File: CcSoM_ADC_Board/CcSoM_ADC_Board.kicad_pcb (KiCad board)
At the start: 4 copper layers, 160 x 100 mm, 158 parts, among them J1 SoM Connector, J12 USB_C_Receptacle_USB2.0_16P, J13 Conn_02x03_Odd_Even, J14 Conn_02x03_Odd_Even, J15 Conn_02x02_Counter_Clockwise, J16 Barrel_Jack, J18 USB_A, J19 USB_A, J3 Conn_02x8_Odd_Even, J4 Conn_Coaxial, J5 HR911130A1, J6 Conn_01x14, J7 Conn_01x08, J8 Conn_01x16_Socket, J9 Conn_01x08, SW3 SW_Push, U1 SN74LVC00APWE4, U10 USB3343, U11 RTL8211E-VB-CG, U14 SN74CB3T3306DCTR, U2 74AUP1G04, U3 93LC46B, U4 FT2232HL, U5 SN74CB3T3245PWR, U6 TPS73625DBV, U7 TPS3307-33DR, U8 TPS73633DBV, X1 12MHz, Y1 25MHz

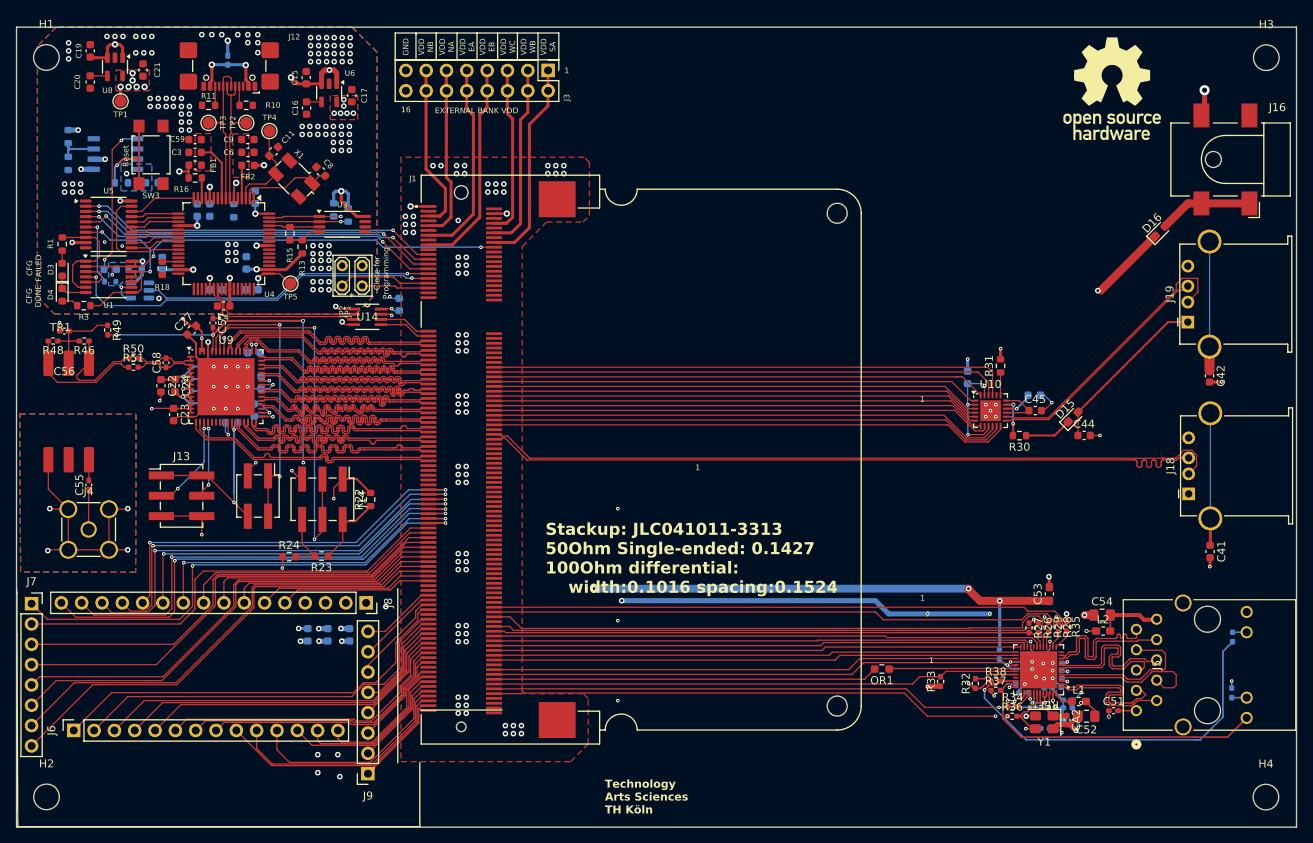
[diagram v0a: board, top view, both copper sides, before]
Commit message: changed from 10Bit ADC to 12Bit
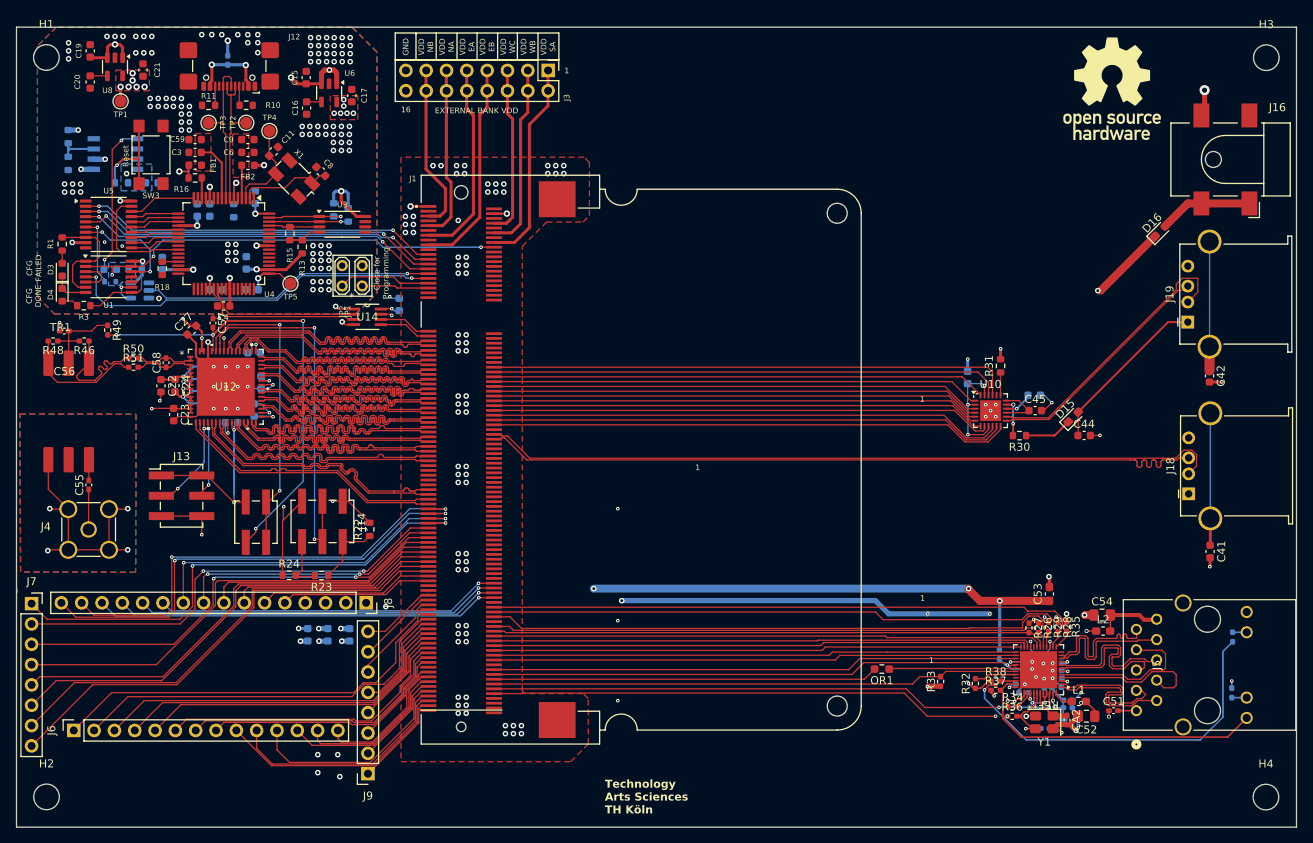
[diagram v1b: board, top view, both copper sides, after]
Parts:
- removed U9: ~, Package_DFN_QFN:QFN-64-1EP_9x9mm_P0.5mm_EP7.15x7.15mm
- added U12: LTC2242IUP-12-PBF, LTC2242-12:QFN-64_UP_LIT, F.Cu at (93.3, 95.5)
- moved R22 3.73 mm to (111.2, 113.3)
- moved J15 3.27 mm to (97.0, 112.4)
- moved J14 2.77 mm to (105.3, 112.3)
- moved R23 2.44 mm to (105.2, 119.1)
- moved R24 2.33 mm to (101.2, 119.1)
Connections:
- J1 pad 107: SB0_N -> D0_P
- J1 pad 109: SB0_P -> D0_N
- J1 pad 111: SB1_N -> OSC_N
- J1 pad 113: SB1_P -> OSC_P
- J1 pad 146: unconnected-(J1D-EB1_P-Pad146) -> EB1_P
- J1 pad 148: unconnected-(J1D-EB1_N-Pad148) -> EB1_N
- J1 pad 150: unconnected-(J1D-EB3_P-Pad150) -> EB3_P
- J1 pad 152: unconnected-(J1D-EB3_N-Pad152) -> EB3_N
- J1 pad 45: OF_N -> OF_P
- J1 pad 47: OF_P -> OF_N
- J1 pad 49: D9_P -> D11_P
- J1 pad 51: D9_N -> D11_N
- J1 pad 53: D8_P -> D10_P
- J1 pad 55: D8_N -> D10_N
- J1 pad 57: D7_P -> D9_P
- J1 pad 59: D7_N -> D9_N
- J1 pad 61: D6_P -> D8_P
- J1 pad 63: D6_N -> D8_N
- J1 pad 65: D5_P -> D7_P
- J1 pad 67: D5_N -> D7_N
- J1 pad 69: D4_P -> D6_P
- J1 pad 71: D4_N -> D6_N
- J1 pad 73: D3_P -> D5_P
- J1 pad 75: D3_N -> D5_N
- J1 pad 81: D2_P -> D4_P
- J1 pad 83: D2_N -> D4_N
- J1 pad 85: D1_P -> D3_P
- J1 pad 87: D1_N -> D3_N
- J1 pad 89: D0_P -> D2_P
- J1 pad 91: D0_N -> D2_N
- J1 pad 93: OSC_N -> D1_P
- J1 pad 95: OSC_P -> D1_N
- J15 pad 3: V_CM -> OVDD
- J15 pad 4: OVDD -> V_CM
- J8 pad 11: SB1_P -> EB1_P
- J8 pad 12: SB0_N -> EB1_N
- J8 pad 13: SB0_P -> EB3_P
- J8 pad 14: SB1_N -> EB3_N
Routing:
- net SB1_N: track 55.5 -> 0.00 mm, vias 2 -> 0
- net SB0_P: track 53.3 -> 0.00 mm, vias 2 -> 0
- net EB3_N: track 0.00 -> 50.6 mm, vias 0 -> 1
- net SB0_N: track 49.7 -> 0.00 mm, vias 2 -> 0
- net EB3_P: track 0.00 -> 48.2 mm, vias 0 -> 1
- net SB1_P: track 46.1 -> 0.00 mm, vias 2 -> 0
- net EB1_N: track 0.00 -> 45.7 mm, vias 0 -> 1
- net EB1_P: track 0.00 -> 43.2 mm, vias 0 -> 1
- net D11_P: track 0.00 -> 33.5 mm
- net D11_N: track 0.00 -> 33.5 mm
- net D10_P: track 0.00 -> 33.5 mm
- net D10_N: track 0.00 -> 33.5 mm
- net OGND: track 109.2 -> 117.8 mm, vias 259 -> 258
- net V_CM: track 54.0 -> 59.4 mm, vias 5 -> 4
- net BAL_P: track 13.1 -> 15.6 mm
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
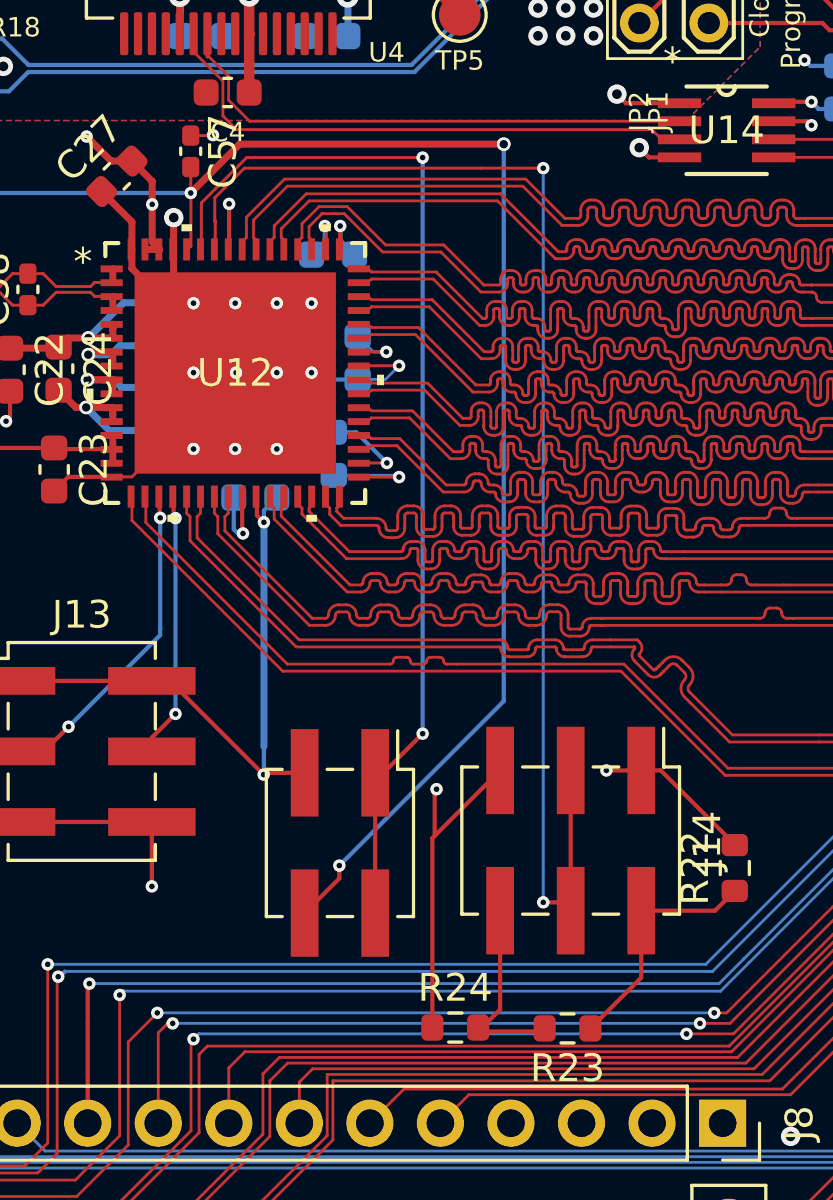
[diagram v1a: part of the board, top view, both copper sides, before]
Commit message: changed some traces
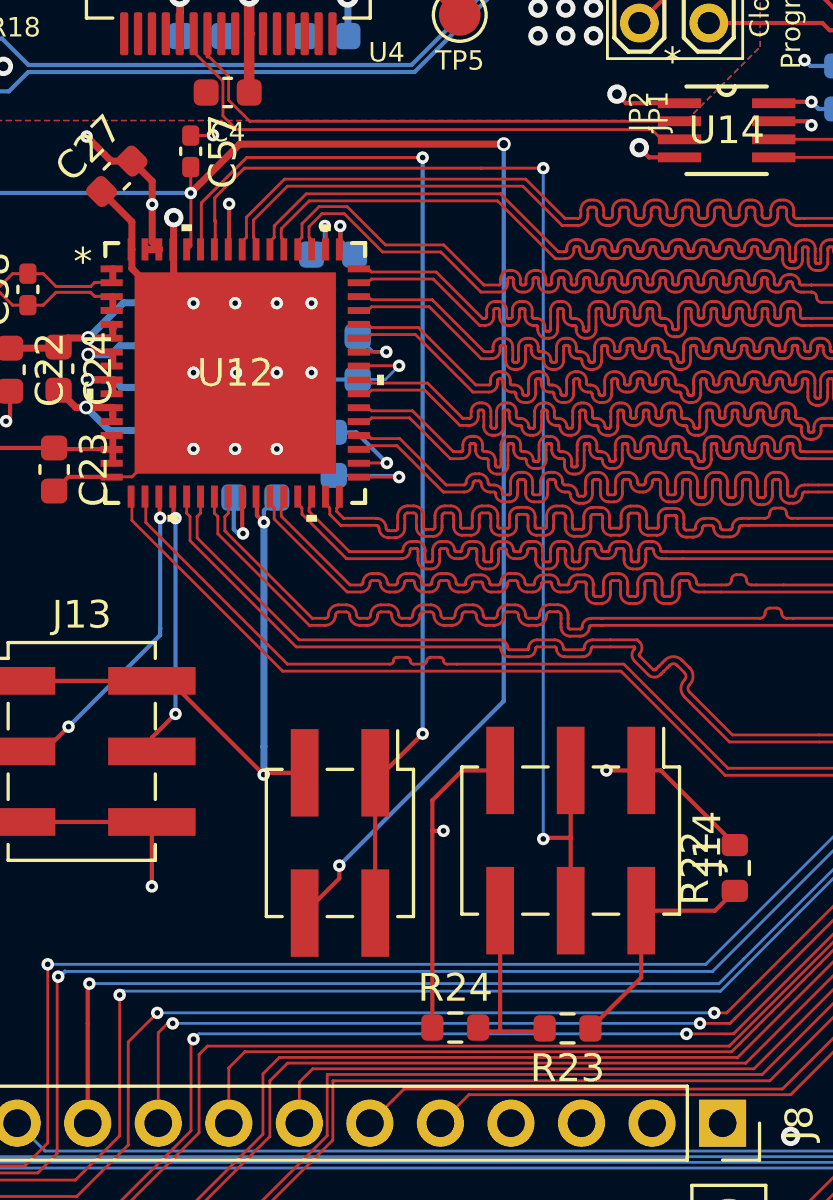
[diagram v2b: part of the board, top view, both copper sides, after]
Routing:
- net Net-(J14-Pin_3): track 46.8 -> 44.8 mm
- net OGND: track 117.8 -> 117.3 mm
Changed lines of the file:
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@@
 		(start 94.284667 108.965333)
 		(end 94.284667 109.965333)
-		(width 0.1524)
+		(width 0.254)
 		(layer "B.Cu")
 		(net 16)
@@
 		(start 97.031879 90.221452)
 		(end 98.691879 91.881452)
-		(width 0.1524)
+		(width 0.254)
 		(layer "In2.Cu")
 		(net 16)
@@
 		(start 92.68133 100.888933)
 		(end 92.160131 101.410131)
-		(width 0.1524)
+		(width 0.254)
 		(layer "In2.Cu")
 		(net 16)
@@
 		(start 91.5 105.25)
 		(end 94.25 108)
-		(width 0.1524)
+		(width 0.635)
 		(layer "In2.Cu")
 		(net 16)
@@
 	)
 	(segment
+		(start 106.614046 109.823942)
+		(end 94.426058 109.823942)
+		(width 0.635)
+		(layer "In2.Cu")
+		(net 16)
+	)
+	(segment
 		(start 82.8535 79.8232)
 		(end 82.8535 81.334114)
@@
 		(start 88.5 105.25)
 		(end 91.5 105.25)
-		(width 0.1524)
+		(width 0.635)
 		(layer "In2.Cu")
 		(net 16)
@@
 	)
 	(segment
-		(start 106.615946 109.825842)
-		(end 94.424158 109.825842)
-		(width 0.1524)
-		(layer "In2.Cu")
-		(net 16)
-	)
-	(segment
 		(start 94.25 109.95)
 		(end 94.275 109.975)
@@
 		(start 97.741455 100.888933)
 		(end 98.711879 99.918509)
-		(width 0.1524)
+		(width 0.254)
 		(layer "In2.Cu")
 		(net 16)
@@
 		(start 94.25 108)
 		(end 94.25 109.95)
-		(width 0.1524)
+		(width 0.635)
 		(layer "In2.Cu")
 		(net 16)
@@
 		(start 98.711879 99.918509)
 		(end 98.711879 98.754)
-		(width 0.1524)
+		(width 0.254)
 		(layer "In2.Cu")
 		(net 16)
@@
 		(start 98.691879 91.881452)
 		(end 98.691879 94.754)
-		(width 0.1524)
+		(width 0.254)
+		(layer "In2.Cu")
+		(net 16)
+	)
+	(segment
+		(start 94.426058 109.823942)
+		(end 94.424158 109.825842)
+		(width 0.635)
 		(layer "In2.Cu")
 		(net 16)
@@
 		(start 94.284667 100.888933)
 		(end 97.741455 100.888933)
-		(width 0.1524)
+		(width 0.254)
 		(layer "In2.Cu")
 		(net 16)
@@
 	)
 	(segment
+		(start 106.615946 109.825842)
+		(end 106.614046 109.823942)
+		(width 0.635)
+		(layer "In2.Cu")
+		(net 16)
+	)
+	(segment
 		(start 94.284667 100.888933)
 		(end 92.68133 100.888933)
-		(width 0.1524)
+		(width 0.254)
 		(layer "In2.Cu")
 		(net 16)
@@
 		(start 92.160131 101.410131)
 		(end 84.666751 101.410131)
-		(width 0.1524)
+		(width 0.635)
 		(layer "In2.Cu")
 		(net 16)
@@
 		(start 84.663441 101.413441)
 		(end 88.5 105.25)
-		(width 0.1524)
+		(width 0.635)
 		(layer "In2.Cu")
 		(net 16)
@@
 		(start 98.691879 94.754)
 		(end 98.691879 98.734)
-		(width 0.1524)
+		(width 0.254)
 		(layer "In2.Cu")
 		(net 16)
@@
 	)
 	(segment
+		(start 102.7902 109.824223)
+		(end 101.425777 109.824223)
+		(width 0.1524)
+		(layer "F.Cu")
+		(net 17)
+	)
+	(segment
 		(start 91.031879 89.925404)
 		(end 91.037581 89.919702)
@@
 	)
 	(segment
-		(start 100.432211 112.182211)
-		(end 100.432211 110.567789)
-		(width 0.1524)
-		(layer "F.Cu")
-		(net 17)
-	)
-	(segment
 		(start 85.144132 96.170487)
 		(end 85.144132 97.105868)
@@
 	)
 	(segment
-		(start 100.432211 110.567789)
-		(end 100.5 110.5)
-		(width 0.1524)
-		(layer "F.Cu")
-		(net 17)
-	)
-	(segment
 		(start 191.005 134.755)
 		(end 191 134.75)
@@
 	)
 	(segment
-		(start 100.35 119.223048)
-		(end 100.35 112.264423)
-		(width 0.1524)
-		(layer "F.Cu")
-		(net 17)
-	)
-	(segment
 		(start 194.462966 136.66377)
 		(end 193.33623 136.66377)
@@
 	)
 	(segment
-		(start 100.432211 112.182211)
-		(end 102.7902 109.824223)
-		(width 0.1524)
-		(layer "F.Cu")
-		(net 17)
-	)
-	(segment
 		(start 188.9 133.45)
 		(end 188.9 133.75)
@@
 	)
 	(segment
+		(start 100.35 112)
+		(end 100.75 112)
+		(width 0.1524)
+		(layer "F.Cu")
+		(net 17)
+	)
+	(segment
 		(start 216.287337 117.962663)
 		(end 216.25 118)
@@
 	)
 	(segment
+		(start 101.425777 109.824223)
+		(end 100.35 110.9)
+		(width 0.1524)
+		(layer "F.Cu")
+		(net 17)
+	)
+	(segment
 		(start 196.2 120.55)
 		(end 196.2 119.3)
@@
 	)
 	(segment
+		(start 100.35 110.9)
+		(end 100.35 112)
+		(width 0.1524)
+		(layer "F.Cu")
+		(net 17)
+	)
+	(segment
 		(start 88.844379 99.254)
 		(end 87.240789 99.254)
@@
 	)
 	(segment
-		(start 100.35 112.264423)
-		(end 100.432211 112.182211)
-		(width 0.1524)
-		(layer "F.Cu")
-		(net 17)
-	)
-	(segment
 		(start 96.531879 90.273055)
 		(end 96.480276 90.221452)
@@
 	)
 	(segment
+		(start 100.35 112)
+		(end 100.35 119.223048)
+		(width 0.1524)
+		(layer "F.Cu")
+		(net 17)
+	)
+	(segment
 		(start 113.8559 86.45)
 		(end 114 86.5941)
@@
 	)
 	(via
-		(at 100.5 110.5)
-		(size 0.45)
-		(drill 0.2)
-		(layers "F.Cu" "B.Cu")
-		(net 17)
-	)
-	(via
 		(at 104.8535 54.8732)
 		(size 0.7)
@@
 	)
 	(via
+		(at 100.75 112)
+		(size 0.45)
+		(drill 0.2)
+		(layers "F.Cu" "B.Cu")
+		(net 17)
+	)
+	(via
 		(at 123.3035 126.3732)
 		(size 0.7)
@@
 	)
 	(segment
+		(start 104.384521 112.25)
+		(end 104.3432 112.291321)
+		(width 0.1524)
+		(layer "F.Cu")
+		(net 119)
+	)
+	(segment
 		(start 92.531879 91.0665)
 		(end 92.511879 91.0465)
@@
 	(segment
 		(start 105.3302 109.824223)
-		(end 105.3302 114.874223)
-		(width 0.1524)
-		(layer "F.Cu")
-		(net 119)
-	)
-	(segment
-		(start 104.3432 114.574552)
-		(end 105.030529 114.574552)
+		(end 105.3302 112.25)
 		(width 0.1524)
 		(layer "F.Cu")
@@
 	)
 	(segment
+		(start 105.3302 112.25)
+		(end 105.3302 114.874223)
+		(width 0.1524)
+		(layer "F.Cu")
+		(net 119)
+	)
+	(segment
 		(start 92.515177 89.204117)
 		(end 93.581294 88.138)
@@
 	)
 	(segment
+		(start 105.3302 112.25)
+		(end 104.384521 112.25)
+		(width 0.1524)
+		(layer "F.Cu")
+		(net 119)
+	)
+	(segment
 		(start 92.531879 90.043)
 		(end 92.515177 90.026298)
@@
 	)
 	(via
-		(at 104.3432 114.574552)
+		(at 104.3432 112.291321)
 		(size 0.45)
 		(drill 0.2)
@@
 	)
 	(segment
+		(start 104.3432 112.291321)
+		(end 104.347033 112.295154)
+		(width 0.108204)
+		(layer "B.Cu")
+		(net 119)
+	)
+	(segment
 		(start 104.3432 88.138)
-		(end 104.3432 114.574552)
+		(end 104.3432 112.291321)
 		(width 0.108204)
 		(layer "B.Cu")
@@
 	(segment
 		(start 102.7902 114.874223)
-		(end 102.7902 118.432848)
+		(end 102.7902 119.182848)
 		(width 0.1524)
 		(layer "F.Cu")
@@
 	)
 	(segment
-		(start 102.7902 118.432848)
-		(end 102 119.223048)
+		(start 102 119.223048)
+		(end 102.75 119.223048)
 		(width 0.1524)
 		(layer "F.Cu")
@@
 	)
 	(segment
-		(start 102 119.223048)
+		(start 102.7902 119.182848)
+		(end 102.75 119.223048)
+		(width 0.1524)
+		(layer "F.Cu")
+		(net 120)
+	)
+	(segment
+		(start 102.75 119.223048)
 		(end 104.282398 119.223048)
 		(width 0.1524)

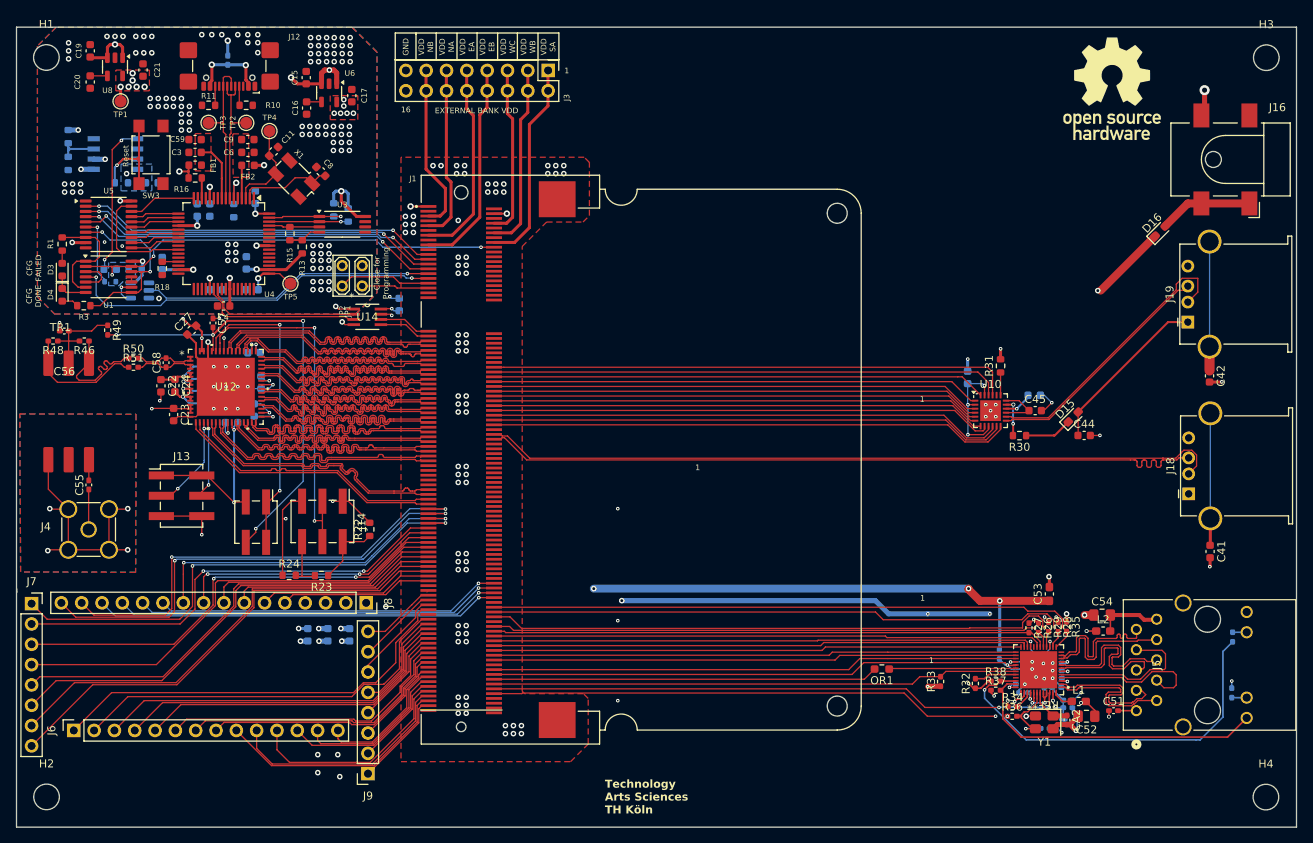
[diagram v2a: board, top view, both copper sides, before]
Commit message: moved designator and changed vddio to 2.5V
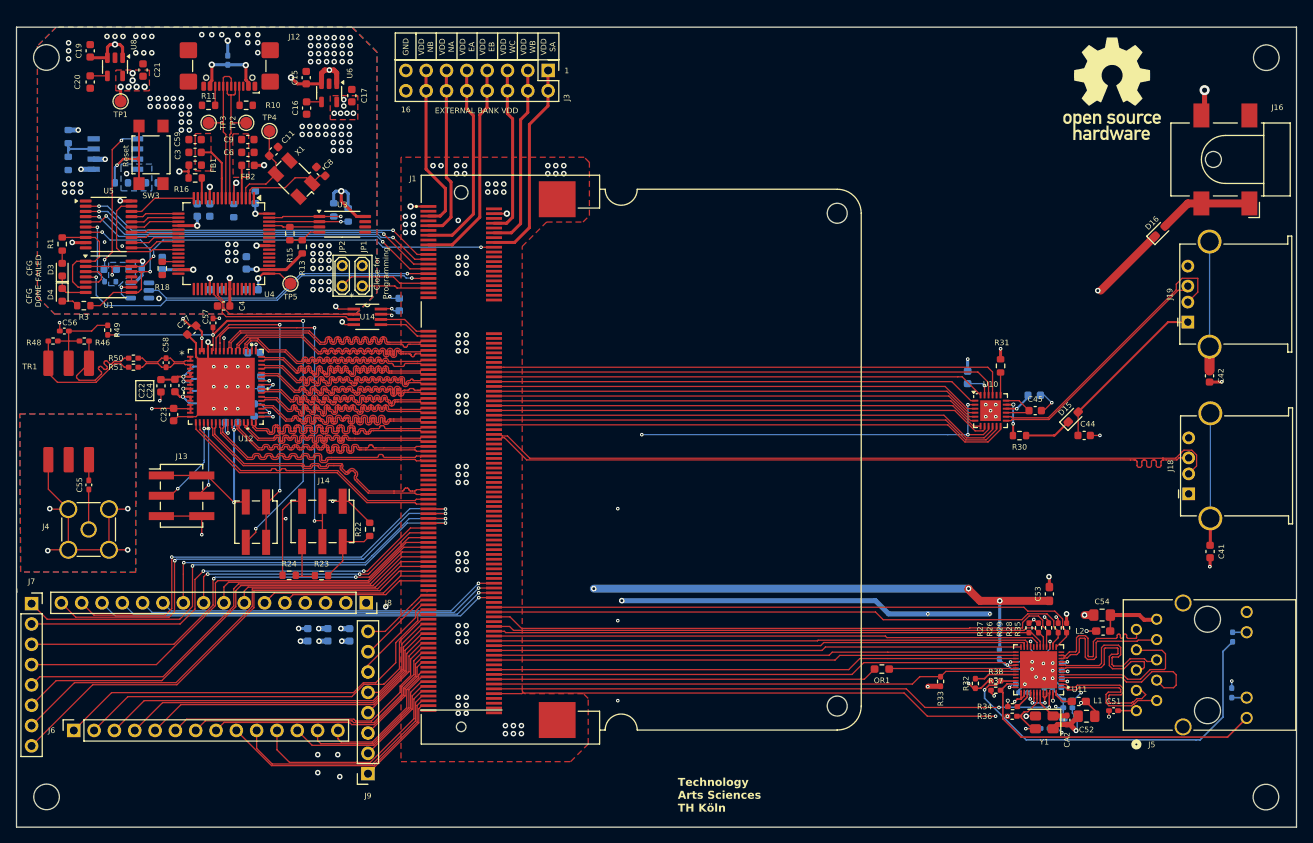
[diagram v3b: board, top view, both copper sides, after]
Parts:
- moved R35 0.15 mm to (198.3, 125.7)
- moved R28 0.10 mm to (197.3, 125.7)
- moved R29 0.10 mm to (196.1, 125.7)
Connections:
- C47 pad 1: USB_CLKOUT -> +1V8
- R22 pad 1: Net-(J14-Pin_2) -> OVDD
- R22 pad 2: OVDD -> Net-(J14-Pin_2)
- U10 pad 2: USB_CLKOUT -> OVDD
- U10 pad 23: USB_CLKOUT -> +1V8
- U10 pad 9: USB_CLKOUT -> OVDD
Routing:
- net OVDD: track 485.7 -> 535.7 mm, vias 29 -> 32
- net USB_CLKOUT: track 14.0 -> 0.00 mm, vias 3 -> 0
- net +1V8: track 0.00 -> 3.41 mm, vias 0 -> 1
